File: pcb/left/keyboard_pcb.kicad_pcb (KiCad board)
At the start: 2 copper layers, 138.8 x 89.9 mm, 34 parts, among them J1 TRRS, K00 KEYSW, K01 KEYSW, K02 KEYSW, K03 KEYSW, K04 KEYSW, K05 KEYSW, K10 KEYSW, K11 KEYSW, K12 KEYSW, K13 KEYSW, K14 KEYSW, K15 KEYSW, K20 KEYSW, K21 KEYSW, K22 KEYSW, K23 KEYSW, K24 KEYSW, K25 KEYSW, K33 KEYSW, K34 KEYSW, K35 KEYSW, U2 Pico

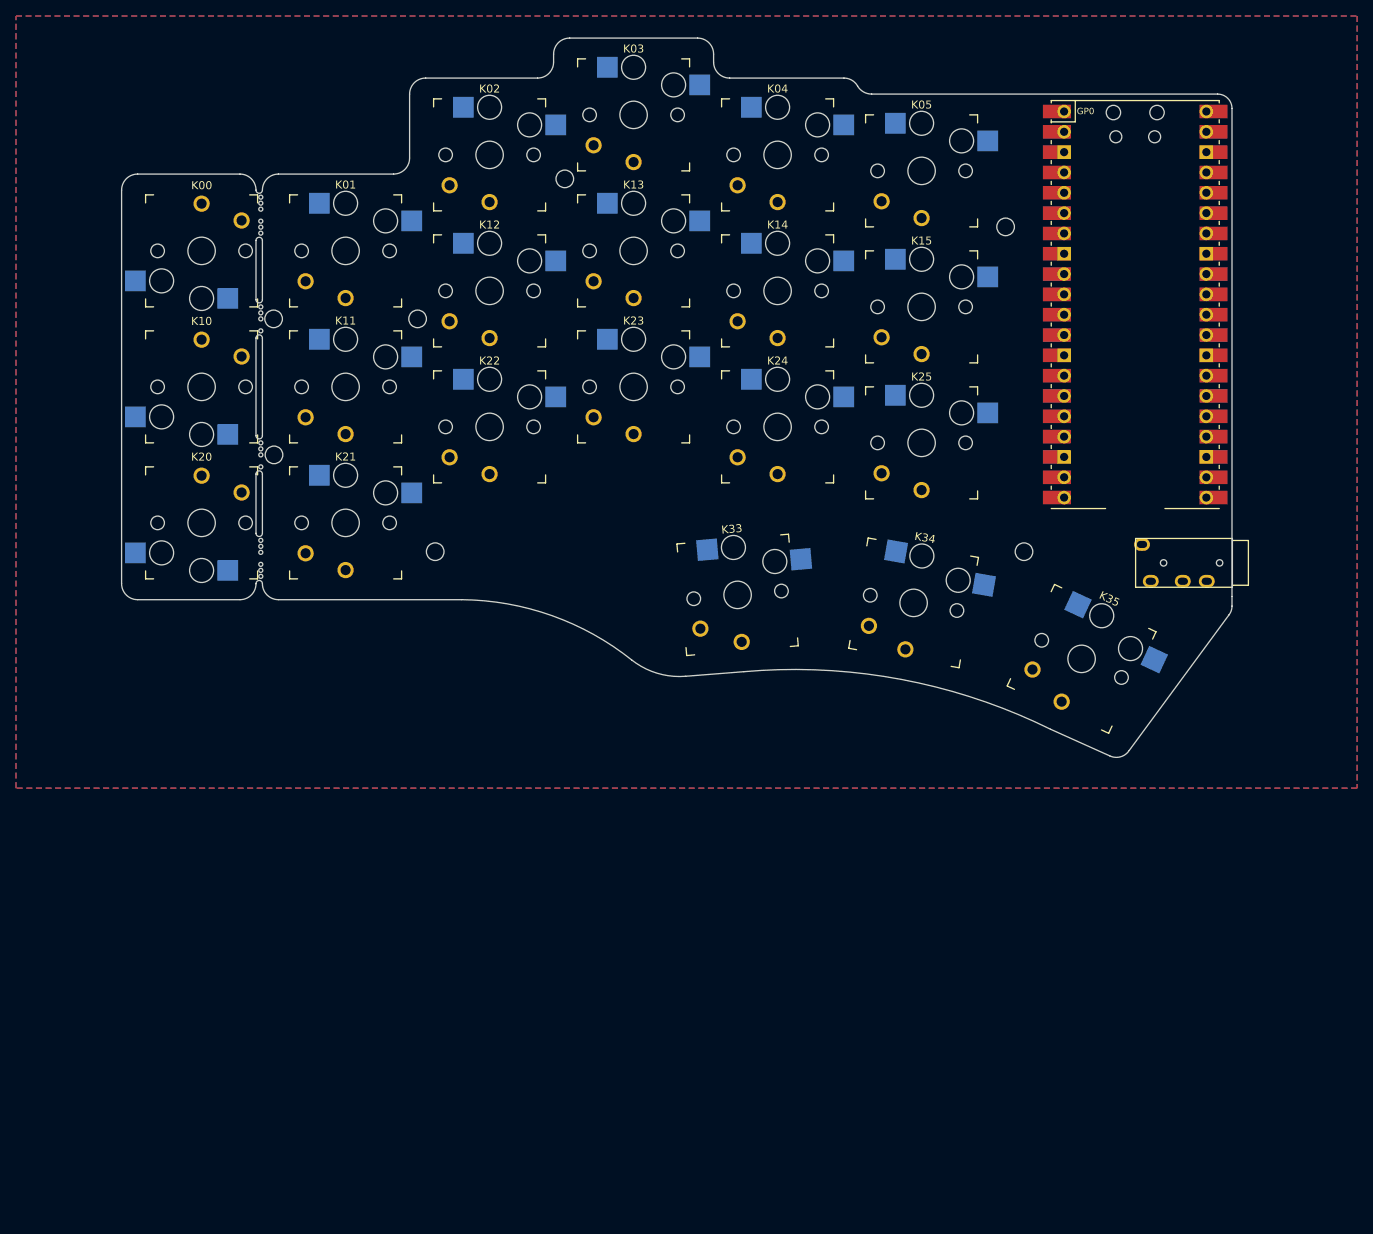
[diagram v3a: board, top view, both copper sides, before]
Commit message: Update PCB from schematic
 * Rotate switches as needed
 * Flip all lefthand footprints to back
 * Fix minor alignment issue in USB socket
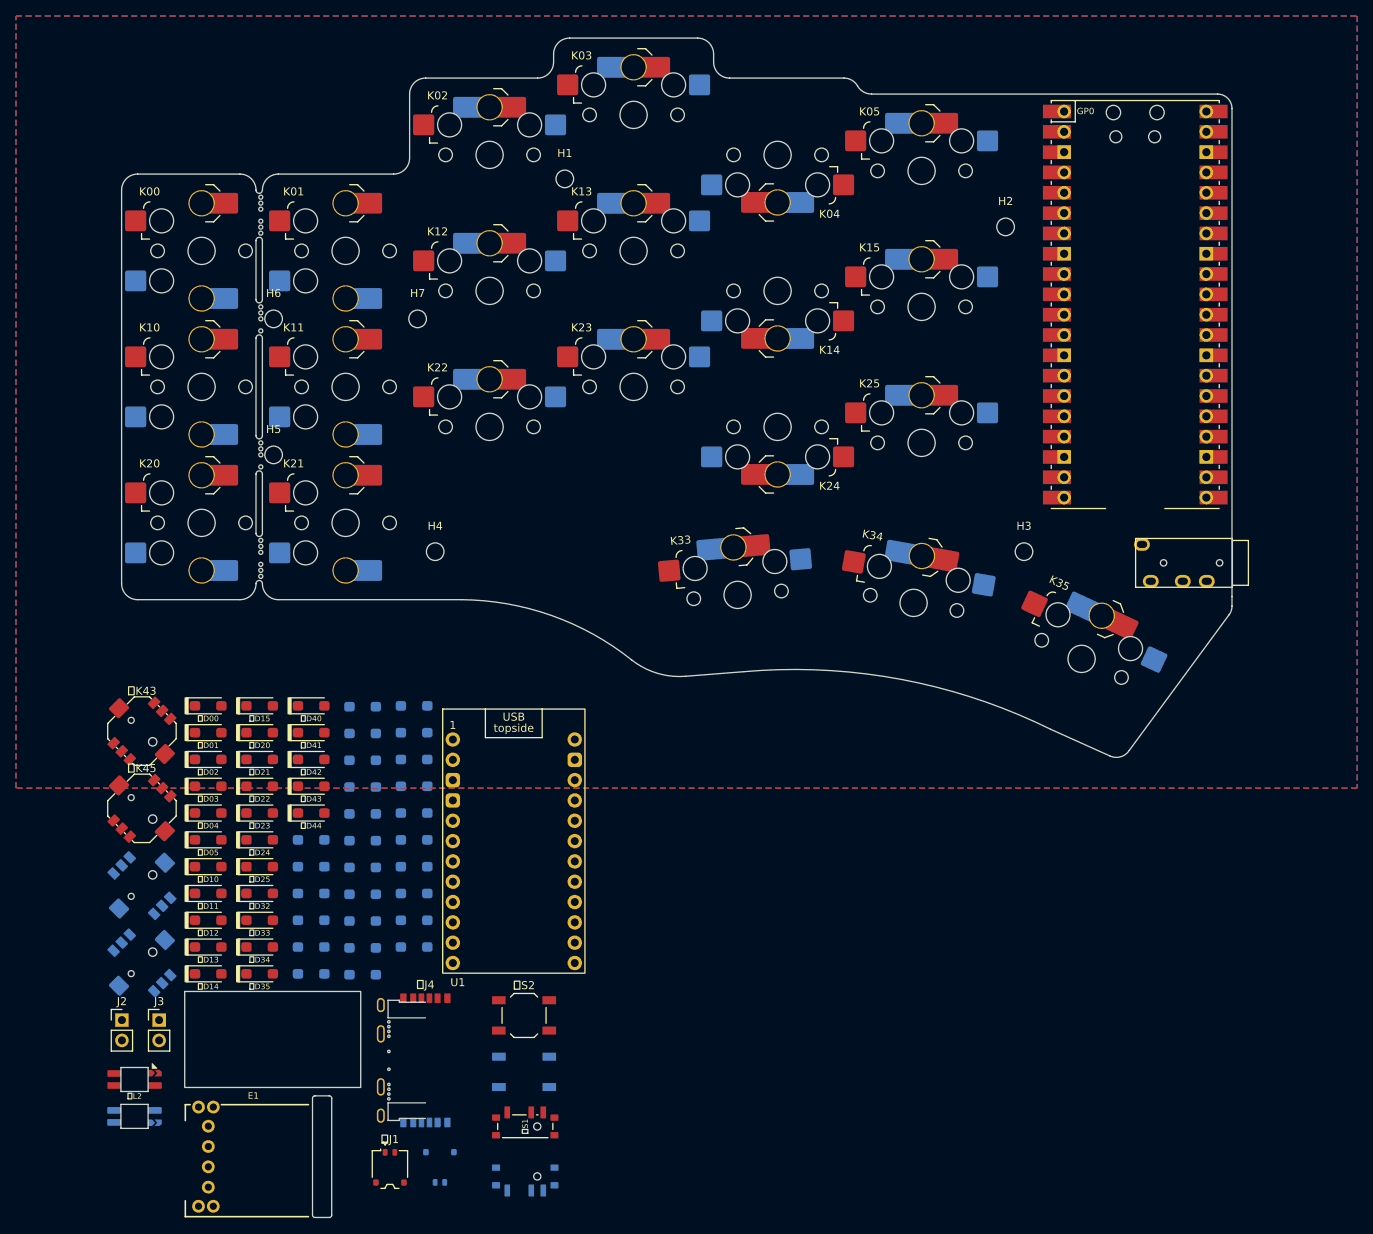
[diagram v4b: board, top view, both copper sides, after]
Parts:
- added B1: MountingHole, ♥Project_Library:Battery_Cutout_401020, F.Cu at (82.9, 168.6)
- added E1: RotaryEncoder_Switch, ♥Project_Library:RollerEncoder_Panasonic_EVQWGD001_Reversible, F.Cu at (80.5, 183.2)
- added J2: Alt. Battery, Connector_PinHeader_2.54mm:PinHeader_1x02_P2.54mm_Vertical, F.Cu at (64.0, 166.2)
- added J3: Alt. Switch, Connector_PinHeader_2.54mm:PinHeader_1x02_P2.54mm_Vertical, F.Cu at (68.7, 166.2)
- added U1: Flippable RP2040 ProMicro/nice!nano, PCM_marbastlib-xp-promicroish:ProMicro_USBup, F.Cu at (113.0, 145.0)
- added 右D00: 1N4148, ♥Project_Library:D_SOD-123, F.Cu at (74.8, 126.9)
- added 右D01: 1N4148, ♥Project_Library:D_SOD-123, F.Cu at (74.8, 130.2)
- added 右D02: 1N4148, ♥Project_Library:D_SOD-123, F.Cu at (74.8, 133.6)
- added 右D03: 1N4148, ♥Project_Library:D_SOD-123, F.Cu at (74.8, 136.9)
- added 右D04: 1N4148, ♥Project_Library:D_SOD-123, F.Cu at (74.8, 140.3)
- added 右D05: 1N4148, ♥Project_Library:D_SOD-123, F.Cu at (74.8, 143.6)
- added 右D10: 1N4148, ♥Project_Library:D_SOD-123, F.Cu at (74.8, 147.0)
- added 右D11: 1N4148, ♥Project_Library:D_SOD-123, F.Cu at (74.8, 150.3)
- added 右D12: 1N4148, ♥Project_Library:D_SOD-123, F.Cu at (74.8, 153.7)
- added 右D13: 1N4148, ♥Project_Library:D_SOD-123, F.Cu at (74.8, 157.0)
- added 右D14: 1N4148, ♥Project_Library:D_SOD-123, F.Cu at (74.8, 160.4)
- added 右D15: 1N4148, ♥Project_Library:D_SOD-123, F.Cu at (81.3, 126.9)
- added 右D20: 1N4148, ♥Project_Library:D_SOD-123, F.Cu at (81.3, 130.2)
- added 右D21: 1N4148, ♥Project_Library:D_SOD-123, F.Cu at (81.3, 133.6)
- added 右D22: 1N4148, ♥Project_Library:D_SOD-123, F.Cu at (81.3, 136.9)
- added 右D23: 1N4148, ♥Project_Library:D_SOD-123, F.Cu at (81.3, 140.3)
- added 右D24: 1N4148, ♥Project_Library:D_SOD-123, F.Cu at (81.3, 143.6)
- added 右D25: 1N4148, ♥Project_Library:D_SOD-123, F.Cu at (81.3, 147.0)
- added 右D32: 1N4148, ♥Project_Library:D_SOD-123, F.Cu at (81.3, 150.3)
- added 右D33: 1N4148, ♥Project_Library:D_SOD-123, F.Cu at (81.3, 153.7)
- added 右D34: 1N4148, ♥Project_Library:D_SOD-123, F.Cu at (81.3, 157.0)
- added 右D35: 1N4148, ♥Project_Library:D_SOD-123, F.Cu at (81.3, 160.4)
- added 右D40: 1N4148, ♥Project_Library:D_SOD-123, F.Cu at (87.7, 126.9)
- added 右D41: 1N4148, ♥Project_Library:D_SOD-123, F.Cu at (87.7, 130.2)
- added 右D42: 1N4148, ♥Project_Library:D_SOD-123, F.Cu at (87.7, 133.6)
- added 右D43: 1N4148, ♥Project_Library:D_SOD-123, F.Cu at (87.7, 136.9)
- added 右D44: 1N4148, ♥Project_Library:D_SOD-123, F.Cu at (87.7, 140.3)
- added 右J1: Conn_01x02_Pin, Connector_Molex:Molex_Pico-EZmate_78171-0002_1x02-1MP_P1.20mm_Vertical, F.Cu at (97.5, 184.6)
- added 右J4: USB_C_Receptacle_PowerOnly_6P, ♥Project_Library:CUI_UJC-HP-L-G-5-MSMT-TR_Reversible_Optional, F.Cu at (102.0, 167.9)
- added 右K43: SW_SP5T, ♥Project_Library:Nav_Switch_SKRHAxE010, F.Cu at (66.5, 130.0)
- added 右K45: SW_SP5T, ♥Project_Library:Nav_Switch_SKRHAxE010, F.Cu at (66.5, 139.7)
- added 右L2: SK6812MINI-E, ♥Project_Library:SK6812-MINI-E_Jumped_GND, F.Cu at (65.6, 173.6)
- added 右S1: SW_SPST, ♥Project_Library:SW_SPDT_PCM12_Reversible, F.Cu at (114.5, 179.1)
- added 右S2: SW_Push, Button_Switch_SMD:SW_SPST_TL3342, F.Cu at (114.3, 165.6)
- added 左D00: 1N4148, ♥Project_Library:D_SOD-123, B.Cu at (87.7, 143.6)
- added 左D01: 1N4148, ♥Project_Library:D_SOD-123, B.Cu at (87.7, 147.0)
- added 左D02: 1N4148, ♥Project_Library:D_SOD-123, B.Cu at (87.7, 150.3)
- added 左D03: 1N4148, ♥Project_Library:D_SOD-123, B.Cu at (87.7, 153.7)
- added 左D04: 1N4148, ♥Project_Library:D_SOD-123, B.Cu at (87.7, 157.0)
- added 左D05: 1N4148, ♥Project_Library:D_SOD-123, B.Cu at (87.7, 160.4)
- added 左D10: 1N4148, ♥Project_Library:D_SOD-123, B.Cu at (94.1, 160.5)
- added 左D11: 1N4148, ♥Project_Library:D_SOD-123, B.Cu at (94.1, 157.1)
- added 左D12: 1N4148, ♥Project_Library:D_SOD-123, B.Cu at (94.1, 153.8)
- added 左D13: 1N4148, ♥Project_Library:D_SOD-123, B.Cu at (94.1, 150.4)
- added 左D14: 1N4148, ♥Project_Library:D_SOD-123, B.Cu at (94.1, 147.1)
- added 左D15: 1N4148, ♥Project_Library:D_SOD-123, B.Cu at (94.1, 143.7)
- added 左D20: 1N4148, ♥Project_Library:D_SOD-123, B.Cu at (94.1, 140.4)
- added 左D21: 1N4148, ♥Project_Library:D_SOD-123, B.Cu at (94.1, 137.0)
- added 左D22: 1N4148, ♥Project_Library:D_SOD-123, B.Cu at (94.1, 133.7)
- added 左D23: 1N4148, ♥Project_Library:D_SOD-123, B.Cu at (94.1, 130.3)
- added 左D24: 1N4148, ♥Project_Library:D_SOD-123, B.Cu at (94.1, 127.0)
- added 左D25: 1N4148, ♥Project_Library:D_SOD-123, B.Cu at (100.6, 126.9)
- added 左D32: 1N4148, ♥Project_Library:D_SOD-123, B.Cu at (100.6, 130.2)
- added 左D33: 1N4148, ♥Project_Library:D_SOD-123, B.Cu at (100.6, 133.6)
- added 左D34: 1N4148, ♥Project_Library:D_SOD-123, B.Cu at (100.6, 136.9)
- added 左D35: 1N4148, ♥Project_Library:D_SOD-123, B.Cu at (100.6, 140.3)
- added 左D40: 1N4148, ♥Project_Library:D_SOD-123, B.Cu at (100.6, 143.6)
- added 左D41: 1N4148, ♥Project_Library:D_SOD-123, B.Cu at (100.6, 147.0)
- added 左D42: 1N4148, ♥Project_Library:D_SOD-123, B.Cu at (100.6, 150.3)
- added 左D43: 1N4148, ♥Project_Library:D_SOD-123, B.Cu at (100.6, 153.7)
- added 左D44: 1N4148, ♥Project_Library:D_SOD-123, B.Cu at (100.6, 157.0)
- added 左J1: Conn_01x02_Pin, Connector_Molex:Molex_Pico-EZmate_78171-0002_1x02-1MP_P1.20mm_Vertical, B.Cu at (103.8, 184.6)
- added 左J4: USB_C_Receptacle_PowerOnly_6P, ♥Project_Library:CUI_UJC-HP-L-G-5-MSMT-TR_Reversible_Optional, B.Cu at (102.0, 174.5)
- added 左K43: SW_SP5T, ♥Project_Library:Nav_Switch_SKRHAxE010, B.Cu at (66.5, 149.3)
- added 左K45: SW_SP5T, ♥Project_Library:Nav_Switch_SKRHAxE010, B.Cu at (66.5, 159.0)
- added 左L1: SK6812MINI-E, ♥Project_Library:SK6812-MINI-E_Jumped_GND, B.Cu at (65.6, 178.2)
- added 左S1: SW_SPST, ♥Project_Library:SW_SPDT_PCM12_Reversible, B.Cu at (114.5, 186.0)
- added 左S2: SW_Push, Button_Switch_SMD:SW_SPST_TL3342, B.Cu at (114.3, 172.6)
- H1, H2, H3, H4, H5, H6, H7: footprint beekeeb_lib:MountingHole_2.2mm_M2-8mm -> MountingHole:MountingHole_2.2mm_M2
- K00, K01, K10, K11, K20, K21: footprint keyswitches:Kailh_socket_PG1350_optional -> ♥Project_Library:SW_choc_v1_HS_1u_Reversible_Opposing
- K02, K03, K04, K05, K12, K13, K14, K15, K22, K23, K24, K25, K33, K34, K35: footprint keyswitches:Kailh_socket_PG1350_optional -> ♥Project_Library:SW_choc_v1_HS_1u_Reversible
- turned K00 to 0 degrees
- turned K04 to 180 degrees
- turned K10 to 0 degrees
- turned K14 to 180 degrees
- turned K20 to 0 degrees
- turned K24 to 180 degrees
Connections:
- K00 pad 1: /k00 -> Net-(右D00-A)
- K00 pad 2: GND -> col0
- K01 pad 1: /k01 -> Net-(右D01-A)
- K01 pad 2: GND -> col1
- K02 pad 1: /k02 -> Net-(右D02-A)
- K02 pad 2: GND -> col2
- K03 pad 1: /k03 -> Net-(右D03-A)
- K03 pad 2: GND -> col3
- K04 pad 1: /k04 -> Net-(右D04-A)
- K04 pad 2: GND -> col4
- K05 pad 1: /k05 -> Net-(右D05-A)
- K05 pad 2: GND -> col5
- K10 pad 1: /k10 -> Net-(右D10-A)
- K10 pad 2: GND -> col0
- K11 pad 1: /k11 -> Net-(右D11-A)
- K11 pad 2: GND -> col1
- K12 pad 1: /k12 -> Net-(右D12-A)
- K12 pad 2: GND -> col2
- K13 pad 1: /k13 -> Net-(右D13-A)
- K13 pad 2: GND -> col3
- K14 pad 1: /k14 -> Net-(右D14-A)
- K14 pad 2: GND -> col4
- K15 pad 1: /k15 -> Net-(右D15-A)
- K15 pad 2: GND -> col5
- K20 pad 1: /k20 -> Net-(右D20-A)
- K20 pad 2: GND -> col0
- K21 pad 1: /k21 -> Net-(右D21-A)
- K21 pad 2: GND -> col1
- K22 pad 1: /k22 -> Net-(右D22-A)
- K22 pad 2: GND -> col2
- K23 pad 1: /k23 -> Net-(右D23-A)
- K23 pad 2: GND -> col3
- K24 pad 1: /k24 -> Net-(右D24-A)
- K24 pad 2: GND -> col4
- K25 pad 1: /k25 -> Net-(右D25-A)
- K25 pad 2: GND -> col5
- K33 pad 1: /k30 -> Net-(右D33-A)
- K33 pad 2: GND -> col3
- K34 pad 1: /k31 -> Net-(右D34-A)
- K34 pad 2: GND -> col4
- K35 pad 1: /k32 -> Net-(右D35-A)
- K35 pad 2: GND -> col5

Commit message: Position key switch diodes and nav. switches, tweak footprint silkscreens
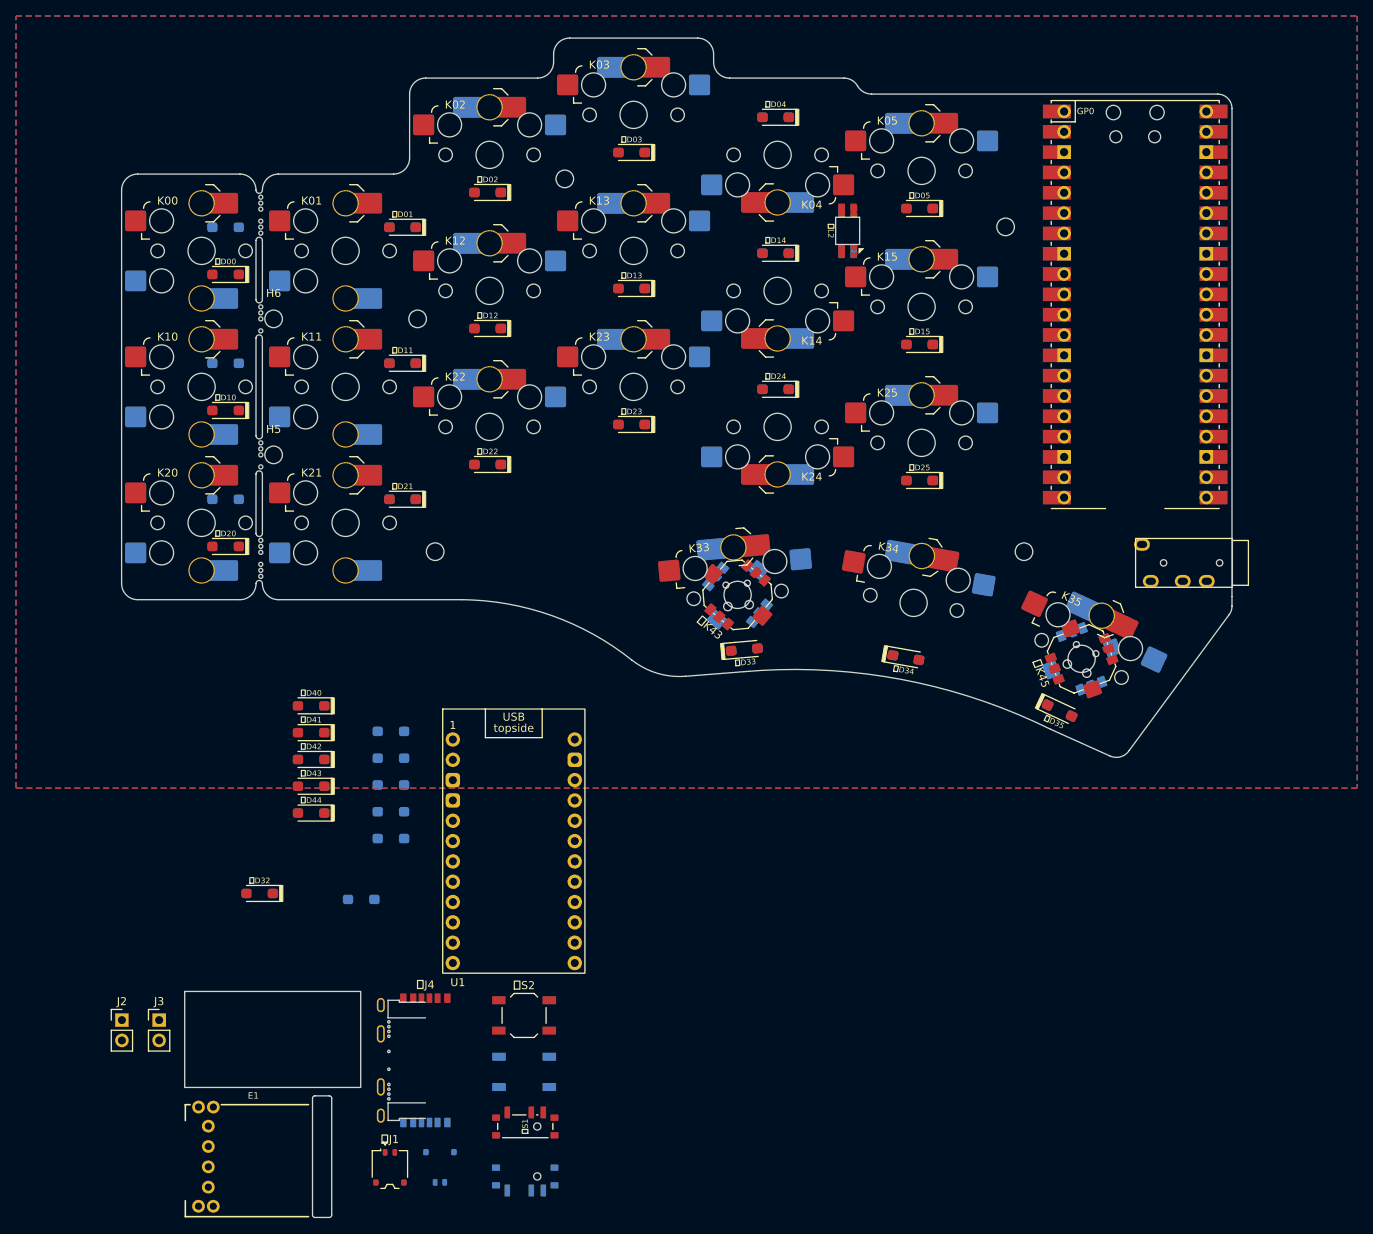
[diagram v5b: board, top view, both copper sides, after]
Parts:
- moved 左L1 142.1 mm to (154.8, 67.5), turned to 90 degrees
- moved 右L2 138.6 mm to (154.8, 67.5), turned to -90 degrees
- moved 左K45 123.4 mm to (184.0, 121.0), turned to 155 degrees
- moved 左D05 122.2 mm to (163.8, 64.7), turned to 180 degrees
- moved 右K45 118.9 mm to (184.0, 121.0), turned to -25 degrees
- moved 右D05 118.9 mm to (163.8, 64.7), turned to 180 degrees
- moved 左D04 118.9 mm to (145.8, 53.3), turned to 180 degrees
- moved 右D14 114.6 mm to (145.8, 70.3), turned to 180 degrees
- moved 右D04 112.2 mm to (145.8, 53.3), turned to 180 degrees
- moved 右D35 105.3 mm to (181.3, 127.5), turned to -25 degrees
- moved 左D03 104.0 mm to (127.8, 57.7), turned to 180 degrees
- moved 右D13 97.9 mm to (127.8, 74.7), turned to 180 degrees
- moved 右D25 95.6 mm to (163.8, 98.7), turned to 180 degrees
- moved 右D03 95.3 mm to (127.8, 57.7), turned to 180 degrees
- moved 右D15 94.1 mm to (163.8, 81.7), turned to 180 degrees
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
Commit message: Replaced RP Pico with Pro Micro/nice!nano footprint
For space reasons, the MCU will be mounted immediately under the main PCB (with no standoffs) with the USB port facing upwards. This requires a cut-out in the PCB to allow space for the USB port and other components.
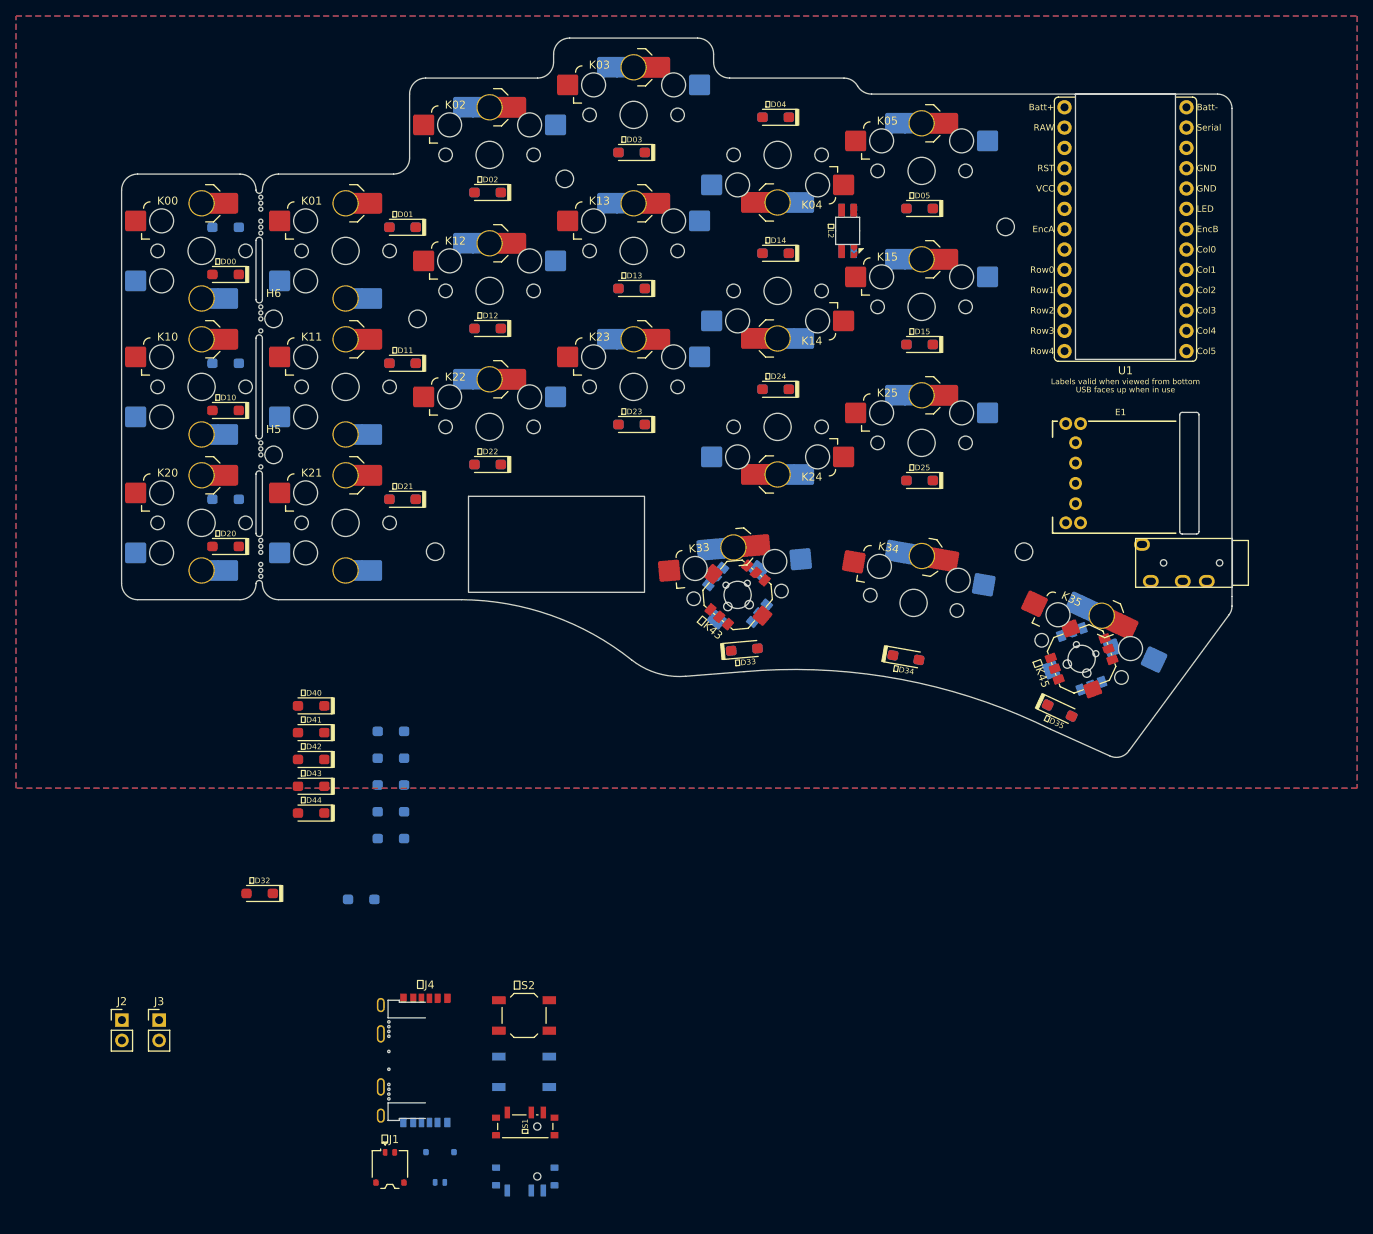
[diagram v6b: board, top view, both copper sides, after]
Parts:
- removed U2: Pico, RPi_Pico:RPi_Pico_SMD_TH
- U1: footprint PCM_marbastlib-xp-promicroish:ProMicro_USBup -> ♥Project_Library:ProMicro_Battery_Reversible
- moved E1 138.0 mm to (188.9, 97.8)
- moved U1 108.1 mm to (189.5, 68.6)
- moved B1 71.3 mm to (118.4, 106.7)
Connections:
- U1 pad 18: unconnected-(U1-GP28/GP3-Pad18) -> enc_b
- U1 pad 7: enc_b -> unconnected-(U1-GP4/GP27-Pad7)
